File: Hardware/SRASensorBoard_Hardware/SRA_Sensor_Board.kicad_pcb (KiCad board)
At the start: 2 copper layers, 124.5 x 81.3 mm, 72 parts, among them J1 USB_A, Q1 BSS138, Q2 BSS138, Q3 BSS138, Q4 BSS138, Q5 Q_PMOS_GDS, Q6 Q_NMOS_GSD, U1 FT230XS, U2 OKI, U3 OKI, U4 TM4C129E_Launchpad

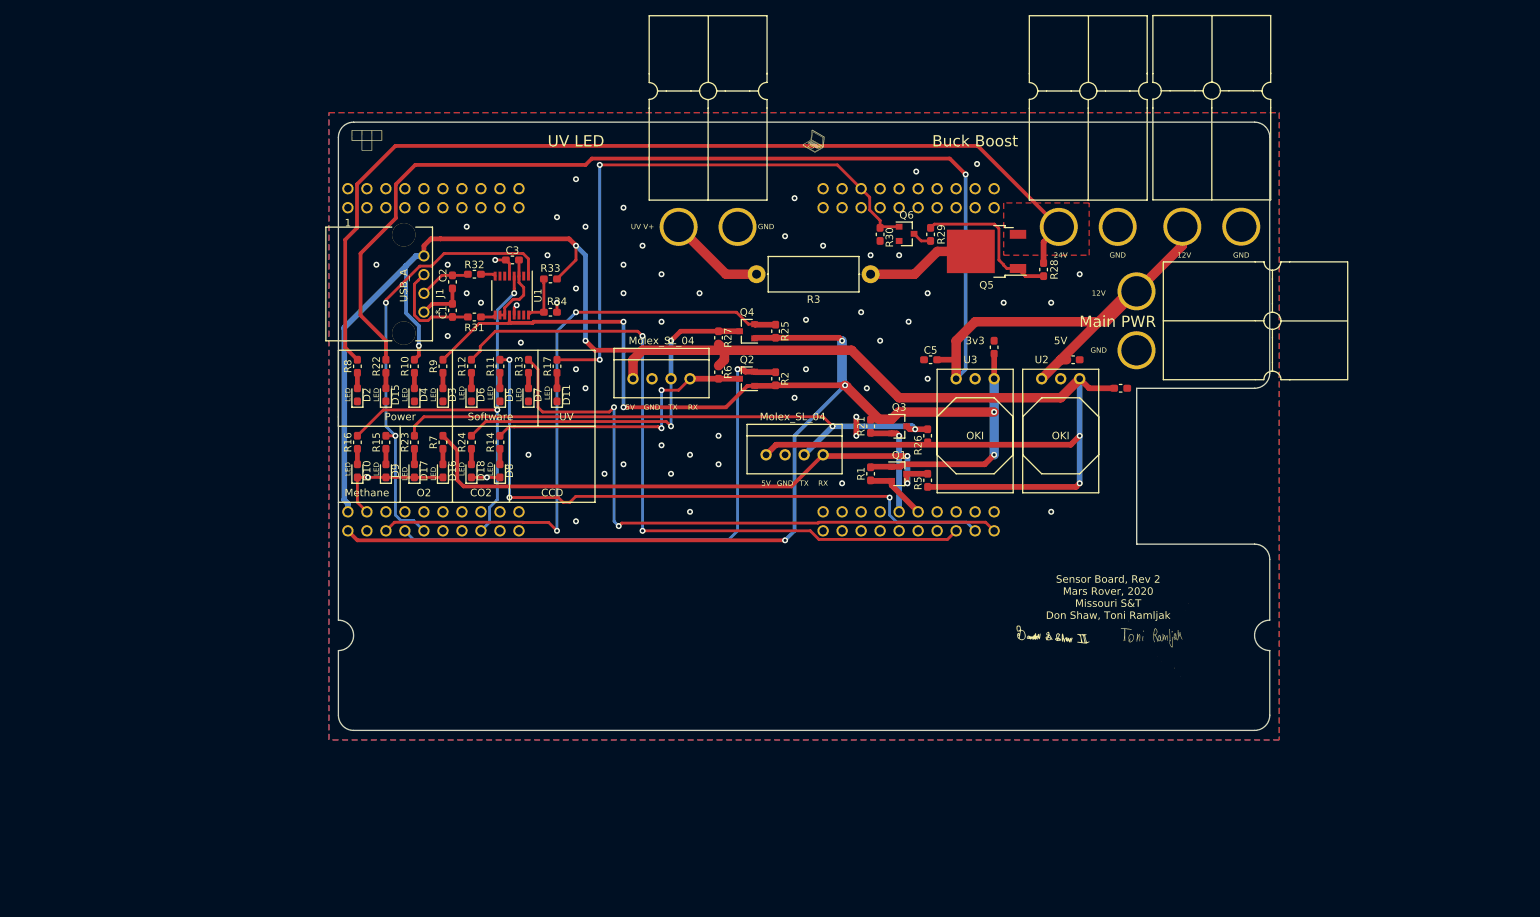
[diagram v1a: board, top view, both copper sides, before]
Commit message: Layout started, edge cut fix
ladybug is not pleased
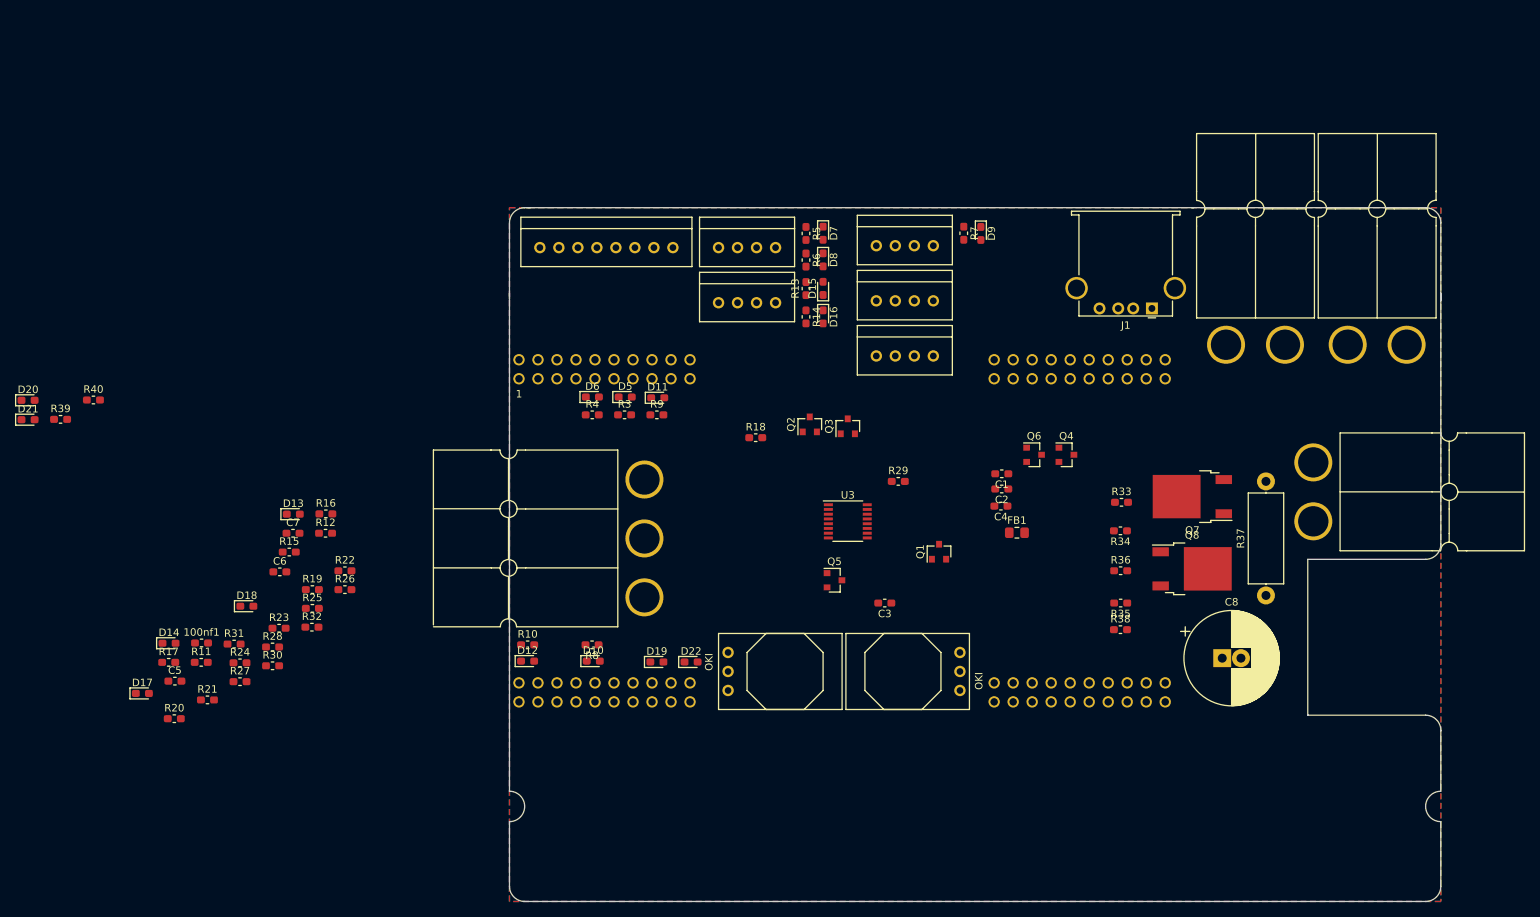
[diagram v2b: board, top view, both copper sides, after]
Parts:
- removed D2, D3, D4: LED, Diode_SMD:D_0603_1608Metric_Pad1.05x0.95mm_HandSolder
- removed G***: LOGO, custom:tetris_silkscreen
- removed G***: LOGO, custom:laptop_medium
- removed G***: LOGO, footprints:Toni_Signature_Rev4
- removed G***: LOGO, custom:Don_Signature_Medium
- removed R1, R2: 10K, Resistor_SMD:R_0603_1608Metric_Pad1.05x0.95mm_HandSolder
- added 100nf1: C, Capacitor_SMD:C_0603_1608Metric_Pad1.05x0.95mm_HandSolder, F.Cu at (50.3, 117.9)
- added C8: 4.7uF, Capacitor_THT:CP_Radial_D12.5mm_P2.50mm, F.Cu at (186.7, 119.9)
- added Conn10: Spectrometer, MRDT_Connectors:MOLEX_SL_08_Vertical, F.Cu at (95.5, 65.0)
- added Conn4: Molex_SL_04, MRDT_Connectors:MOLEX_SL_04_Vertical, F.Cu at (119.4, 65.0)
- added Conn8: Molex_SL_04, MRDT_Connectors:MOLEX_SL_04_Vertical, F.Cu at (119.4, 72.4)
- added Conn9: UV_led, MRDT_Connectors:Anderson_2_Horizontal_Side_by_Side, F.Cu at (198.9, 101.6)
- added D12: LED, Diode_SMD:D_0603_1608Metric_Pad1.05x0.95mm_HandSolder, F.Cu at (93.9, 120.3)
- added D13: LED, Diode_SMD:D_0603_1608Metric_Pad1.05x0.95mm_HandSolder, F.Cu at (62.6, 100.6)
- added D14: LED, Diode_SMD:D_0603_1608Metric_Pad1.05x0.95mm_HandSolder, F.Cu at (45.9, 117.9)
- added D19: LED, Diode_SMD:D_0603_1608Metric_Pad1.05x0.95mm_HandSolder, F.Cu at (111.1, 120.4)
- added D20: LED, Diode_SMD:D_0603_1608Metric_Pad1.05x0.95mm_HandSolder, F.Cu at (27.1, 85.4)
- added D21: LED, Diode_SMD:D_0603_1608Metric_Pad1.05x0.95mm_HandSolder, F.Cu at (27.1, 88.0)
- added D22: LED, Diode_SMD:D_0603_1608Metric_Pad1.05x0.95mm_HandSolder, F.Cu at (115.7, 120.4)
- added FB1: MI0805K601R-10, Resistor_SMD:R_0805_2012Metric_Pad1.15x1.40mm_HandSolder, F.Cu at (159.2, 103.1)
- added Q7: Q_PMOS_GDS, Package_TO_SOT_SMD:TO-252-2, F.Cu at (182.7, 98.3)
- added Q8: Q_NMOS_GSD, Package_TO_SOT_SMD:TO-252-2, F.Cu at (182.7, 107.9)
- added R18: 10K, Resistor_SMD:R_0603_1608Metric_Pad1.05x0.95mm_HandSolder, F.Cu at (124.3, 90.4)
- added R19: 10K, Resistor_SMD:R_0603_1608Metric_Pad1.05x0.95mm_HandSolder, F.Cu at (65.1, 110.7)
- added R20: 10K, Resistor_SMD:R_0603_1608Metric_Pad1.05x0.95mm_HandSolder, F.Cu at (46.7, 128.0)
- added R35: 330, Resistor_SMD:R_0603_1608Metric_Pad1.05x0.95mm_HandSolder, F.Cu at (173.1, 112.5)
- added R36: 10k, Resistor_SMD:R_0603_1608Metric_Pad1.05x0.95mm_HandSolder, F.Cu at (173.1, 108.2)
- added R37: 4, Resistor_THT:R_Axial_DIN0414_L11.9mm_D4.5mm_P15.24mm_Horizontal, F.Cu at (192.5, 111.5)
- added R38: 330, Resistor_SMD:R_0603_1608Metric_Pad1.05x0.95mm_HandSolder, F.Cu at (173.1, 116.1)
- added R39: 330, Resistor_SMD:R_0603_1608Metric_Pad1.05x0.95mm_HandSolder, F.Cu at (31.5, 88.0)
- added R4: 2500, Resistor_SMD:R_0603_1608Metric_Pad1.05x0.95mm_HandSolder, F.Cu at (102.5, 87.4)
- added R40: 330, Resistor_SMD:R_0603_1608Metric_Pad1.05x0.95mm_HandSolder, F.Cu at (35.8, 85.4)
- C1, C2: value 47pF -> 10uF
- C3: value 100nf -> 10uF
- C5, C6: value 10uF -> 47pF
- C7: value 10uF -> 100nf
- Conn1: value Molex_SL_04 -> AndersonPP; footprint MRDT_Connectors:MOLEX_SL_04_Vertical -> MRDT_Connectors:Anderson_3_Horizontal_Side_by_Side
- Conn2: value AndersonPP -> Boost 12V
- Conn3: value Molex_SL_04 -> Boost 24V; footprint MRDT_Connectors:MOLEX_SL_04_Vertical -> MRDT_Connectors:Anderson_2_Horizontal_Side_by_Side
- Conn5: value Boost 12V -> Molex_SL_04; footprint MRDT_Connectors:Anderson_2_Horizontal_Side_by_Side -> MRDT_Connectors:MOLEX_SL_04_Vertical
- Conn6: value Boost 24V -> Molex_SL_04; footprint MRDT_Connectors:Anderson_2_Horizontal_Side_by_Side -> MRDT_Connectors:MOLEX_SL_04_Vertical
- Conn7: value UV_led -> Molex_SL_04; footprint MRDT_Connectors:Anderson_2_Horizontal_Side_by_Side -> MRDT_Connectors:MOLEX_SL_04_Vertical
- J1: footprint custom:292303-1 -> Connector_USB:USB_A_Stewart_SS-52100-001_Horizontal
- Q5: value Q_PMOS_GDS -> BSS138; footprint Package_TO_SOT_SMD:TO-252-2 -> Package_TO_SOT_SMD:SOT-23
- Q6: value Q_NMOS_GSD -> BSS138
- R10: value 510 -> 330
- R15, R16: value 330 -> 27
- R17, R23, R24: value 330 -> 10K
- R22: value 1000 -> 10K
- R26: value 10K -> 4.7k
- R27: value 10K -> 10k
- R28, R29: value 22k -> 10K
- R3: value 2 -> 1000; footprint Resistor_THT:R_Axial_DIN0414_L11.9mm_D4.5mm_P15.24mm_Horizontal -> Resistor_SMD:R_0603_1608Metric_Pad1.05x0.95mm_HandSolder
- R30: value 10k -> 10K
- R31, R32: value 27 -> 330
- R33: value 4.7k -> 22k
- R34: value 10k -> 22k
- R5, R6: value 10K -> 330
- R8: value 2500 -> 330
- U1: value FT230XS -> OKI; footprint Package_SO:SSOP-16_3.9x4.9mm_P0.635mm -> MRDT_Devices:OKI_Horizontal
- U3: value OKI -> FT230XS; footprint MRDT_Devices:OKI_Horizontal -> Package_SO:SSOP-16_3.9x4.9mm_P0.635mm
- moved C6 115.0 mm to (60.8, 108.4)
- moved R28 114.7 mm to (59.8, 118.4), turned to 0 degrees
- moved C5 109.7 mm to (46.7, 123.0), turned to 0 degrees
- moved Conn3 103.5 mm to (211.3, 78.0), turned to 270 degrees
- moved R30 99.6 mm to (59.8, 120.9), turned to 0 degrees
- moved C7 96.9 mm to (62.5, 103.2), turned to 0 degrees
- moved R21 95.9 mm to (51.1, 125.5), turned to 0 degrees
- moved J1 95.3 mm to (177.3, 73.2), turned to 180 degrees
- moved D9 85.6 mm to (154.4, 63.1), turned to 270 degrees
- moved R33 81.9 mm to (173.2, 99.1)
- moved R34 81.6 mm to (173.1, 102.9), turned to 180 degrees
- moved R26 80.5 mm to (69.5, 110.7), turned to 0 degrees
- moved R27 78.7 mm to (55.4, 123.0), turned to 0 degrees
- moved C2 78.4 mm to (157.2, 97.3), turned to 180 degrees
- moved C1 76.6 mm to (157.2, 95.2), turned to 180 degrees
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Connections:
- net Reset renamed Net-(U4-PadPM3)
- C1 pad 1: USB_Data- -> +12V
- C2 pad 1: USB_Data+ -> +12V
- C3 pad 1: Net-(C3-Pad1) -> +5V
- C4 pad 1: +12V -> +3V3
- C5 pad 1: +12V -> Net-(C5-Pad1)
- C6 pad 1: +5V -> Net-(C6-Pad1)
- C7 pad 1: +3V3 -> Net-(C7-Pad1)
- Conn1 pad 1: +5V -> GND
- Conn1 pad 2: GND -> +12V
- Conn1 pad 3: O2_TX -> +12VA
- Conn2 pad 2: +12V -> +12VA
- Conn3 pad 1: +5V -> GND
- Conn3 pad 2: GND -> +24V
- Conn5 pad 1: GND -> +3V3
- Conn5 pad 2: +12V -> GND
- Conn6 pad 1: GND -> +5V
- Conn6 pad 2: +24V -> GND
- Conn7 pad 1: GND -> +12V
- Conn7 pad 2: Net-(Conn7-Pad2) -> GND
- J1 pad 1: +5V -> Net-(FB1-Pad2)
- J1 pad 2: USB_Data- -> Net-(C5-Pad1)
- J1 pad 3: USB_Data+ -> Net-(C6-Pad1)
- Q1 pad 2: TIVA_O2_TX -> N2O_TX
- Q1 pad 3: O2_RX -> N2O_RX
- Q2 pad 2: TIVA_CO2_TX -> TIVA_O2_TX
- Q2 pad 3: C02_RX -> O2_RX
- Q3 pad 2: TIVA_O2_RX -> TIVA_CO2_TX
- Q3 pad 3: O2_TX -> C02_RX
- Q4 pad 2: TIVA_CO2_RX -> N2O_RX
- Q4 pad 3: C02_TX -> N2O_TX
- Q5 pad 1: Net-(Q5-Pad1) -> +3V3
- Q5 pad 2: Net-(Q5-Pad2) -> TIVA_O2_RX
- Q5 pad 3: +24V -> O2_TX
- Q6 pad 1: LED_Enable -> +3V3
- Q6 pad 2: GND -> TIVA_CO2_RX
- Q6 pad 3: Net-(Q6-Pad3) -> C02_TX
- R10 pad 1: +5V -> CO2_RX
- R11 pad 1: SW_Flag2 -> N2O_TX
- R11 pad 2: Net-(D5-Pad2) -> Net-(D13-Pad2)
- R12 pad 1: SW_Flag1 -> N2O_RX
- R12 pad 2: Net-(D6-Pad2) -> Net-(D14-Pad2)
- R13 pad 1: SW_ERROR -> NO2_TX
- R13 pad 2: Net-(D7-Pad2) -> Net-(D15-Pad2)
- R14 pad 1: C02_RX -> NO2_RX
- R14 pad 2: Net-(D8-Pad2) -> Net-(D16-Pad2)
- R15 pad 1: TIVA_USB_RX -> Net-(R15-Pad1)
- R15 pad 2: Net-(D9-Pad2) -> Net-(C5-Pad1)
- R16 pad 1: TIVA_USB_TX -> Net-(R16-Pad1)
- R16 pad 2: Net-(D10-Pad2) -> Net-(C6-Pad1)
- R17 pad 1: LED_Enable -> +3V3
- R17 pad 2: Net-(D11-Pad2) -> N2O_TX
- R21 pad 1: +3V3 -> +5V
- R21 pad 2: TIVA_O2_RX -> O2_RX
- R22 pad 1: +12V -> +5V
- R22 pad 2: Net-(D15-Pad2) -> C02_RX
- R23 pad 1: O2_TX -> +3V3
- R23 pad 2: Net-(D17-Pad2) -> N2O_RX
- R24 pad 1: C02_TX -> +3V3
- R24 pad 2: Net-(D18-Pad2) -> TIVA_O2_RX
- R26 pad 1: +5V -> Net-(R26-Pad1)
- R26 pad 2: O2_TX -> +5V
- R27 pad 1: +5V -> Net-(R26-Pad1)
- R27 pad 2: C02_TX -> GND
- R28 pad 1: +24V -> +12V
- R28 pad 2: Net-(Q5-Pad1) -> N2O_TX
- R29 pad 1: Net-(Q5-Pad1) -> +5V
- R29 pad 2: Net-(Q6-Pad3) -> O2_TX
- R3 pad 1: Net-(Q5-Pad2) -> +12VA
- R3 pad 2: Net-(Conn7-Pad2) -> Net-(D5-Pad2)
- R30 pad 1: GND -> +5V
- R30 pad 2: LED_Enable -> C02_TX
- R31 pad 1: Net-(R31-Pad1) -> TIVA_USB_RX
- R31 pad 2: USB_Data- -> Net-(D17-Pad2)
- R32 pad 1: Net-(R32-Pad1) -> TIVA_USB_TX
- R32 pad 2: USB_Data+ -> Net-(D18-Pad2)
- R33 pad 1: Net-(R33-Pad1) -> +24V
- R33 pad 2: +5V -> Net-(Q7-Pad1)
- R34 pad 1: Net-(R33-Pad1) -> Net-(Q7-Pad1)
- R34 pad 2: GND -> Net-(Q8-Pad3)
- R5 pad 1: +5V -> O2_TX
- R5 pad 2: O2_RX -> Net-(D7-Pad2)
- R6 pad 1: +5V -> O2_RX
- R6 pad 2: C02_RX -> Net-(D8-Pad2)
- R7 pad 1: O2_RX -> NO_SCL
- R7 pad 2: Net-(D16-Pad2) -> Net-(D9-Pad2)
- R8 pad 1: +24V -> NO_SDA
- R8 pad 2: Net-(D2-Pad2) -> Net-(D10-Pad2)
- R9 pad 1: +3V3 -> CO2_TX
- R9 pad 2: Net-(D3-Pad2) -> Net-(D11-Pad2)
- U1 pad 1: TIVA_USB_RX -> +12V
- U1 pad 2: Net-(U1-Pad2) -> GND
- U1 pad 3: Net-(C3-Pad1) -> +5V
- U2 pad 3: +5V -> +3V3
- U3 pad 1: +12V -> TIVA_USB_RX
- U3 pad 2: GND -> Net-(U3-Pad2)
- U3 pad 3: +3V3 -> Net-(C7-Pad1)
- U4 pad +5V: +5V -> Net-(U4-Pad+5V)
- U4 pad PA4: Net-(U4-PadPA4) -> NO2_RX
- U4 pad PA5: Net-(U4-PadPA5) -> NO2_TX
- U4 pad PA6: Net-(U4-PadPA6) -> Clock_Pulse
- U4 pad PB2: Net-(U4-PadPB2) -> NO_SCL
- U4 pad PB3: Net-(U4-PadPB3) -> NO_SDA
- U4 pad PD2: Net-(U4-PadPD2) -> EOS
- U4 pad PD7: Net-(U4-PadPD7) -> Video
- U4 pad PM4: Net-(U4-PadPM4) -> Trigger_Pulse
- U4 pad PM5: Net-(U4-PadPM5) -> Start_Pulse
- U4 pad PP0: Net-(U4-PadPP0) -> N2O_RX
- U4 pad PP1: Net-(U4-PadPP1) -> N2O_TX
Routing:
- net +5V: track 254.8 -> 0.00 mm, vias 5 -> 0
- net +3V3: track 227.7 -> 0.00 mm, vias 7 -> 0
- net +12V: track 199.6 -> 0.00 mm, vias 1 -> 0
- net +24V: track 130.8 -> 0.00 mm
- net SW_Flag1: track 94.0 -> 0.00 mm, vias 2 -> 0
- net SW_Flag2: track 85.8 -> 0.00 mm, vias 3 -> 0
- net SW_ERROR: track 84.6 -> 0.00 mm, vias 2 -> 0
- net TIVA_CO2_RX: track 81.4 -> 0.00 mm, vias 2 -> 0
- net O2_TX: track 77.8 -> 0.00 mm, vias 2 -> 0
- net LED_Enable: track 76.9 -> 0.00 mm, vias 2 -> 0
- net O2_RX: track 76.8 -> 0.00 mm, vias 2 -> 0
- net TIVA_CO2_TX: track 72.3 -> 0.00 mm, vias 1 -> 0
- net TIVA_USB_RX: track 59.4 -> 0.00 mm, vias 2 -> 0
- net TIVA_USB_TX: track 56.0 -> 0.00 mm, vias 2 -> 0
- net C02_TX: track 48.8 -> 0.00 mm, vias 2 -> 0
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- removed copper zone on F.Cu, net +24V
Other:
- board size 124.5 x 81.3 mm -> 124.5 x 92.7 mm
- board text removed: "12V"
- board text removed: "24V"
- board text removed: "3v3"
- board text removed: "5V"
- board text removed: "Buck Boost"
- board text removed: "CCD"
- board text removed: "CO2"
- board text removed: "GND"
- board text removed: "Main PWR"
- board text removed: "Methane"
- board text removed: "O2"
- board text removed: "Power"
- board text removed: "RX"
- board text removed: "Sensor Board, Rev 2 Mars Rover, 2020 Missouri S&T Don Shaw, Toni Ramljak"
- board text removed: "Software"
- board text removed: "TX"
- board text removed: "UV"
- board text removed: "UV LED"
- board text removed: "UV V+"

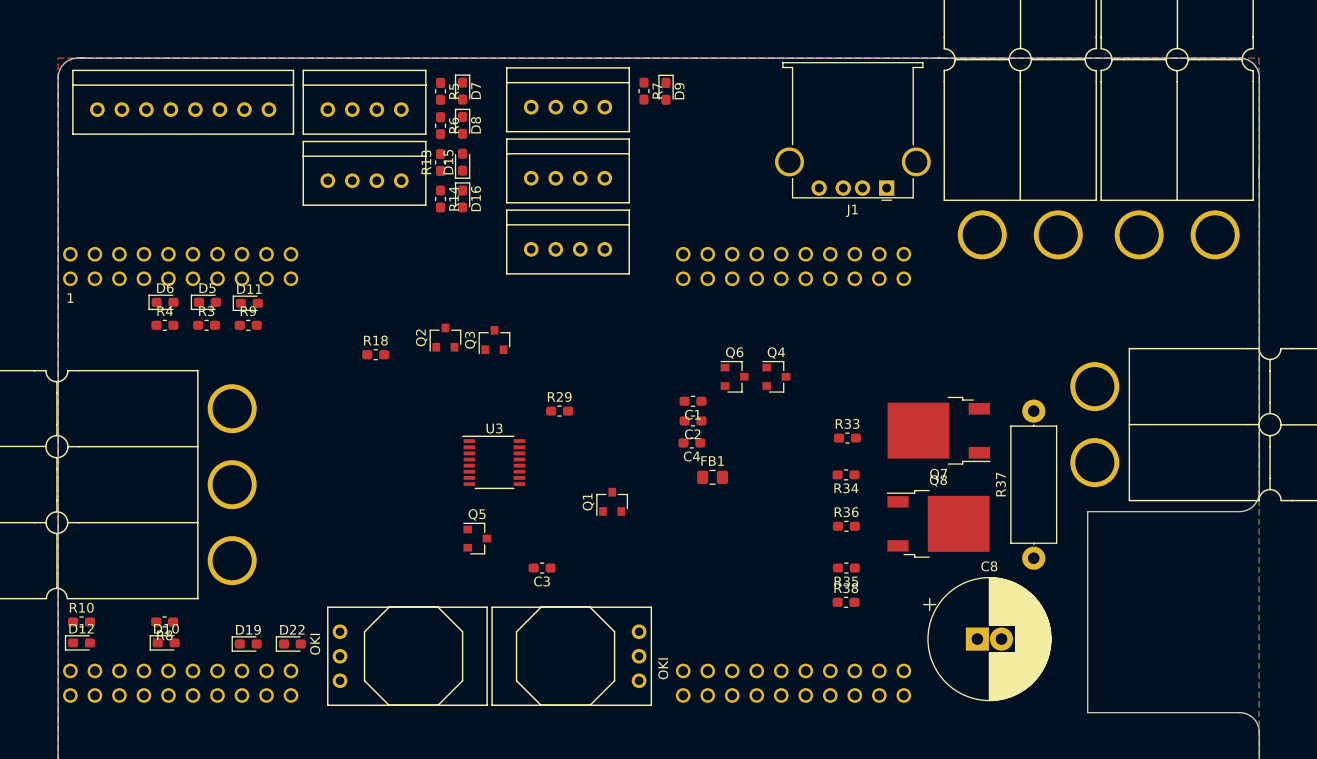
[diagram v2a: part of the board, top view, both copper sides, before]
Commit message: edge cuts fixed
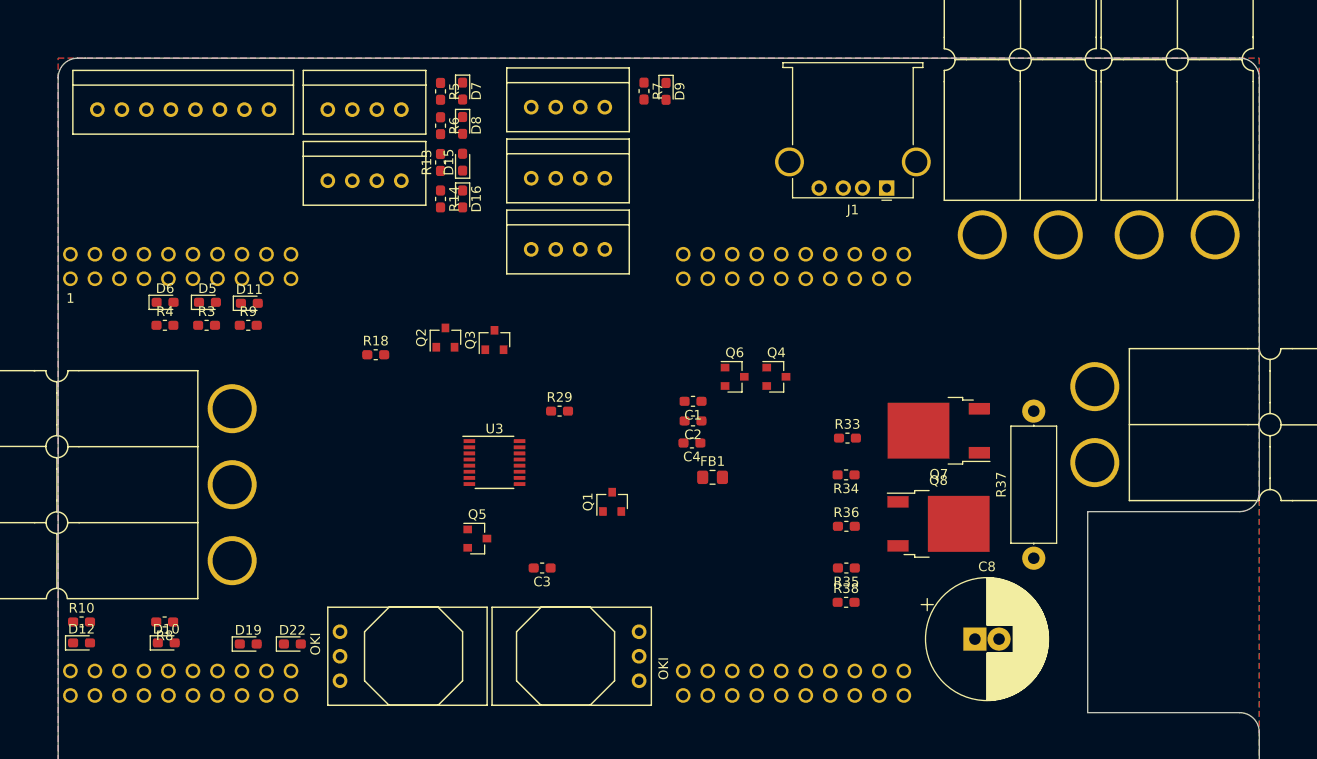
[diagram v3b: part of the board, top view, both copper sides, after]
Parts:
- moved C8 0.25 mm to (186.4, 119.9)
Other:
- outline, holes or cut-outs redrawn
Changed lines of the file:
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@@
-(kicad_pcb (version 20171130) (host pcbnew "(5.1.5)-3")
+(kicad_pcb (version 20171130) (host pcbnew "(5.1.4)-1")
   (general
     (thickness 1.6)
-    (drawings 22)
+    (drawings 20)
     (tracks 0)
     (zones 0)
@@
   )
   (module Capacitor_THT:CP_Radial_D12.5mm_P2.50mm (layer F.Cu)
-    (at 186.69 119.888)
+    (at 186.436 119.888)
     (descr "CP, Radial series, Radial, pin pitch=2.50mm, , diameter=12.5mm, Electrolytic Capacitor")
     (tags "CP Radial series Radial pin pitch 2.50mm  diameter 12.5mm Electrolytic Capacitor")
@@
     )
   )
+  (gr_line (start 213.868 59.69) (end 94.234 59.69) (layer Edge.Cuts) (width 0.05))
+  (gr_line (start 215.9 61.722) (end 215.9 104.648) (layer Edge.Cuts) (width 0.05))
+  (gr_line (start 91.44 71.12) (end 91.44 61.722) (layer Edge.Cuts) (width 0.05))
   (gr_arc (start 213.868 61.722) (end 215.9 61.722) (angle -90) (layer Edge.Cuts) (width 0.05))
-  (gr_line (start 215.9 72.136) (end 215.9 61.722) (layer Edge.Cuts) (width 0.05))
-  (gr_line (start 182.626 59.69) (end 213.868 59.69) (layer Edge.Cuts) (width 0.05))
   (gr_arc (start 93.472 61.722) (end 93.472 59.69) (angle -90) (layer Edge.Cuts) (width 0.05))
   (gr_line (start 94.234 59.69) (end 93.472 59.69) (layer Edge.Cuts) (width 0.05))
-  (gr_line (start 182.88 59.69) (end 93.726 59.69) (layer Edge.Cuts) (width 0.05))
-  (gr_line (start 91.44 71.882) (end 91.44 61.722) (layer Edge.Cuts) (width 0.05))
-  (gr_line (start 215.9 104.648) (end 215.9 71.12) (layer Edge.Cuts) (width 0.05))
   (gr_arc (start 213.868 104.648) (end 213.868 106.68) (angle -90) (layer Edge.Cuts) (width 0.05))
   (gr_line (start 198.12 106.68) (end 213.868 106.68) (layer Edge.Cuts) (width 0.05))
